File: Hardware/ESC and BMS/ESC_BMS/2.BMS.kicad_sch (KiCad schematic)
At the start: 39 parts, among them J301 SW IN, J302 SW OUT, Q301 SQJ141ELP, Q302 SQJ141ELP, Q303 FDV304P, Q304 PMV20XNEA, Q305 SQJ141ELP, U301 BQ2057W, U302 BQ2969

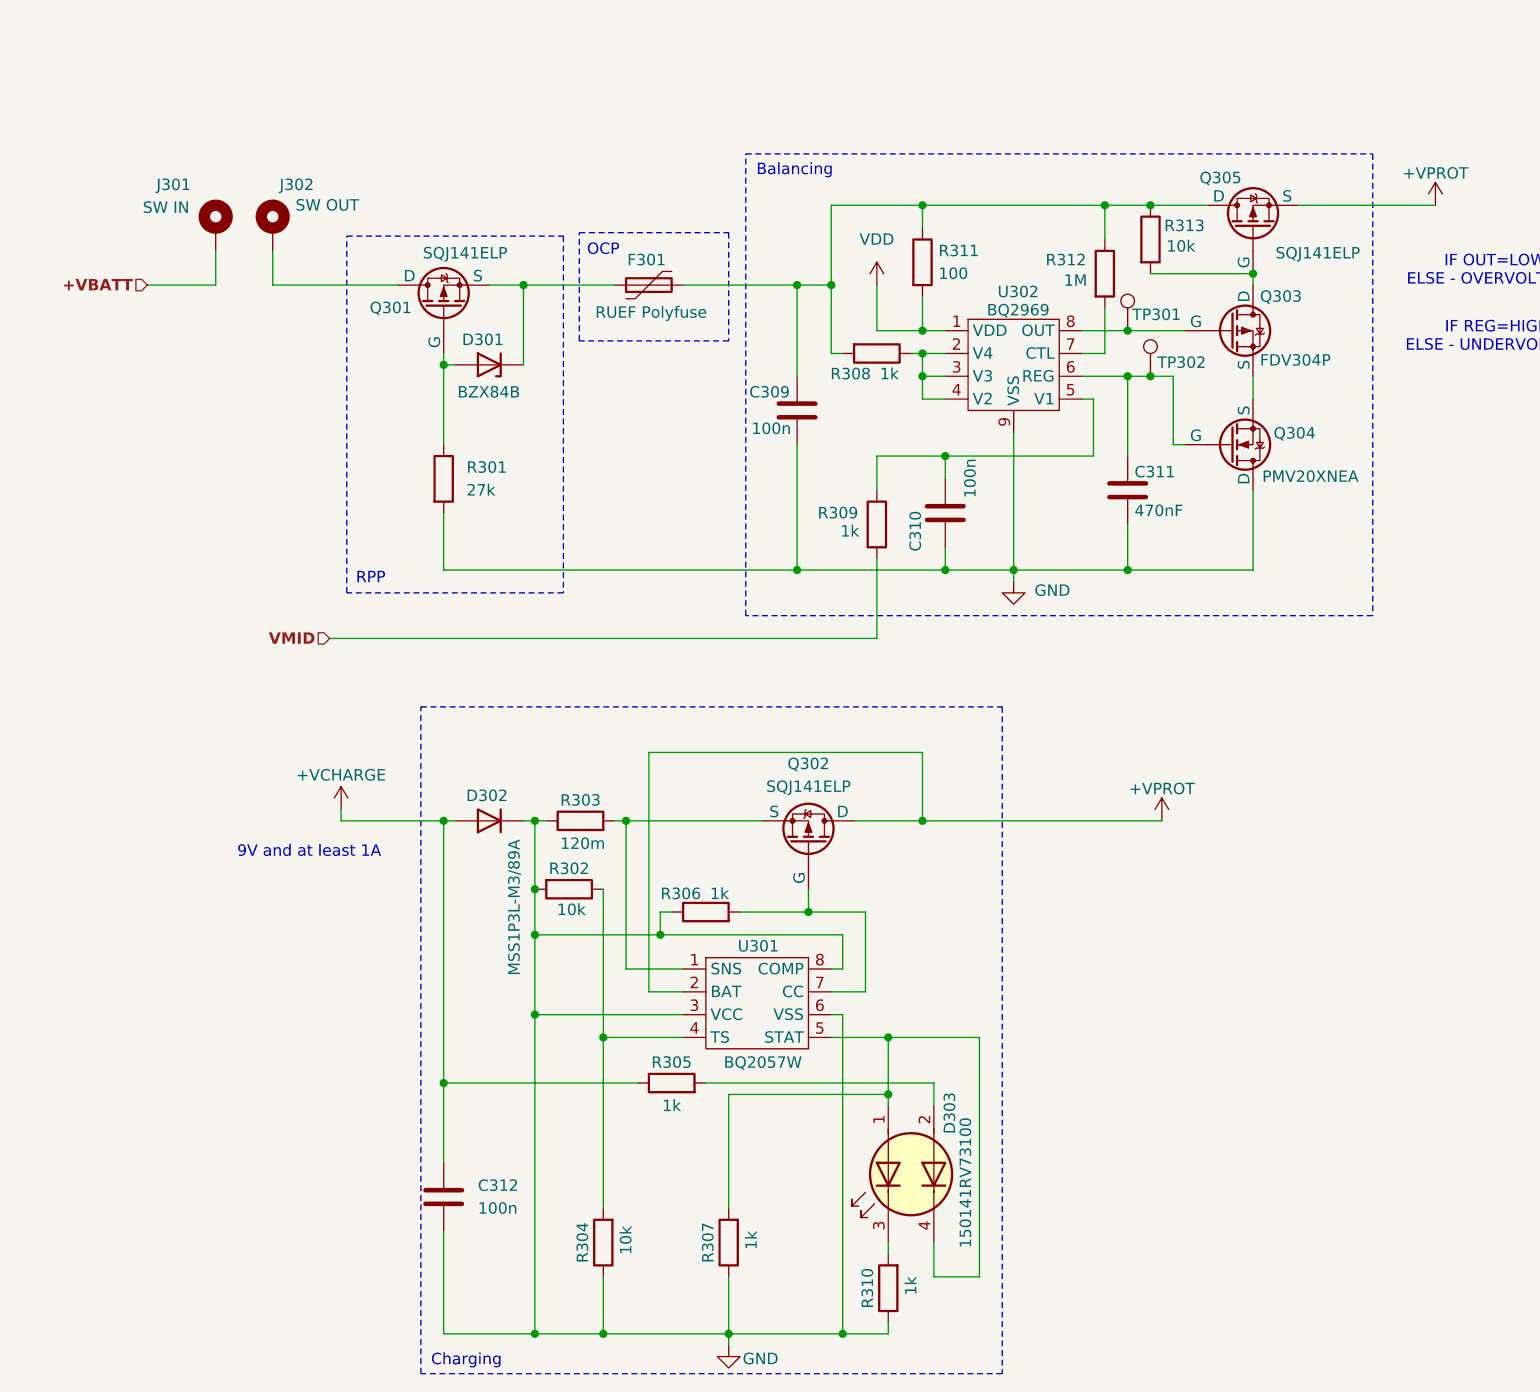
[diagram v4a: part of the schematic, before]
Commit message: ESC done
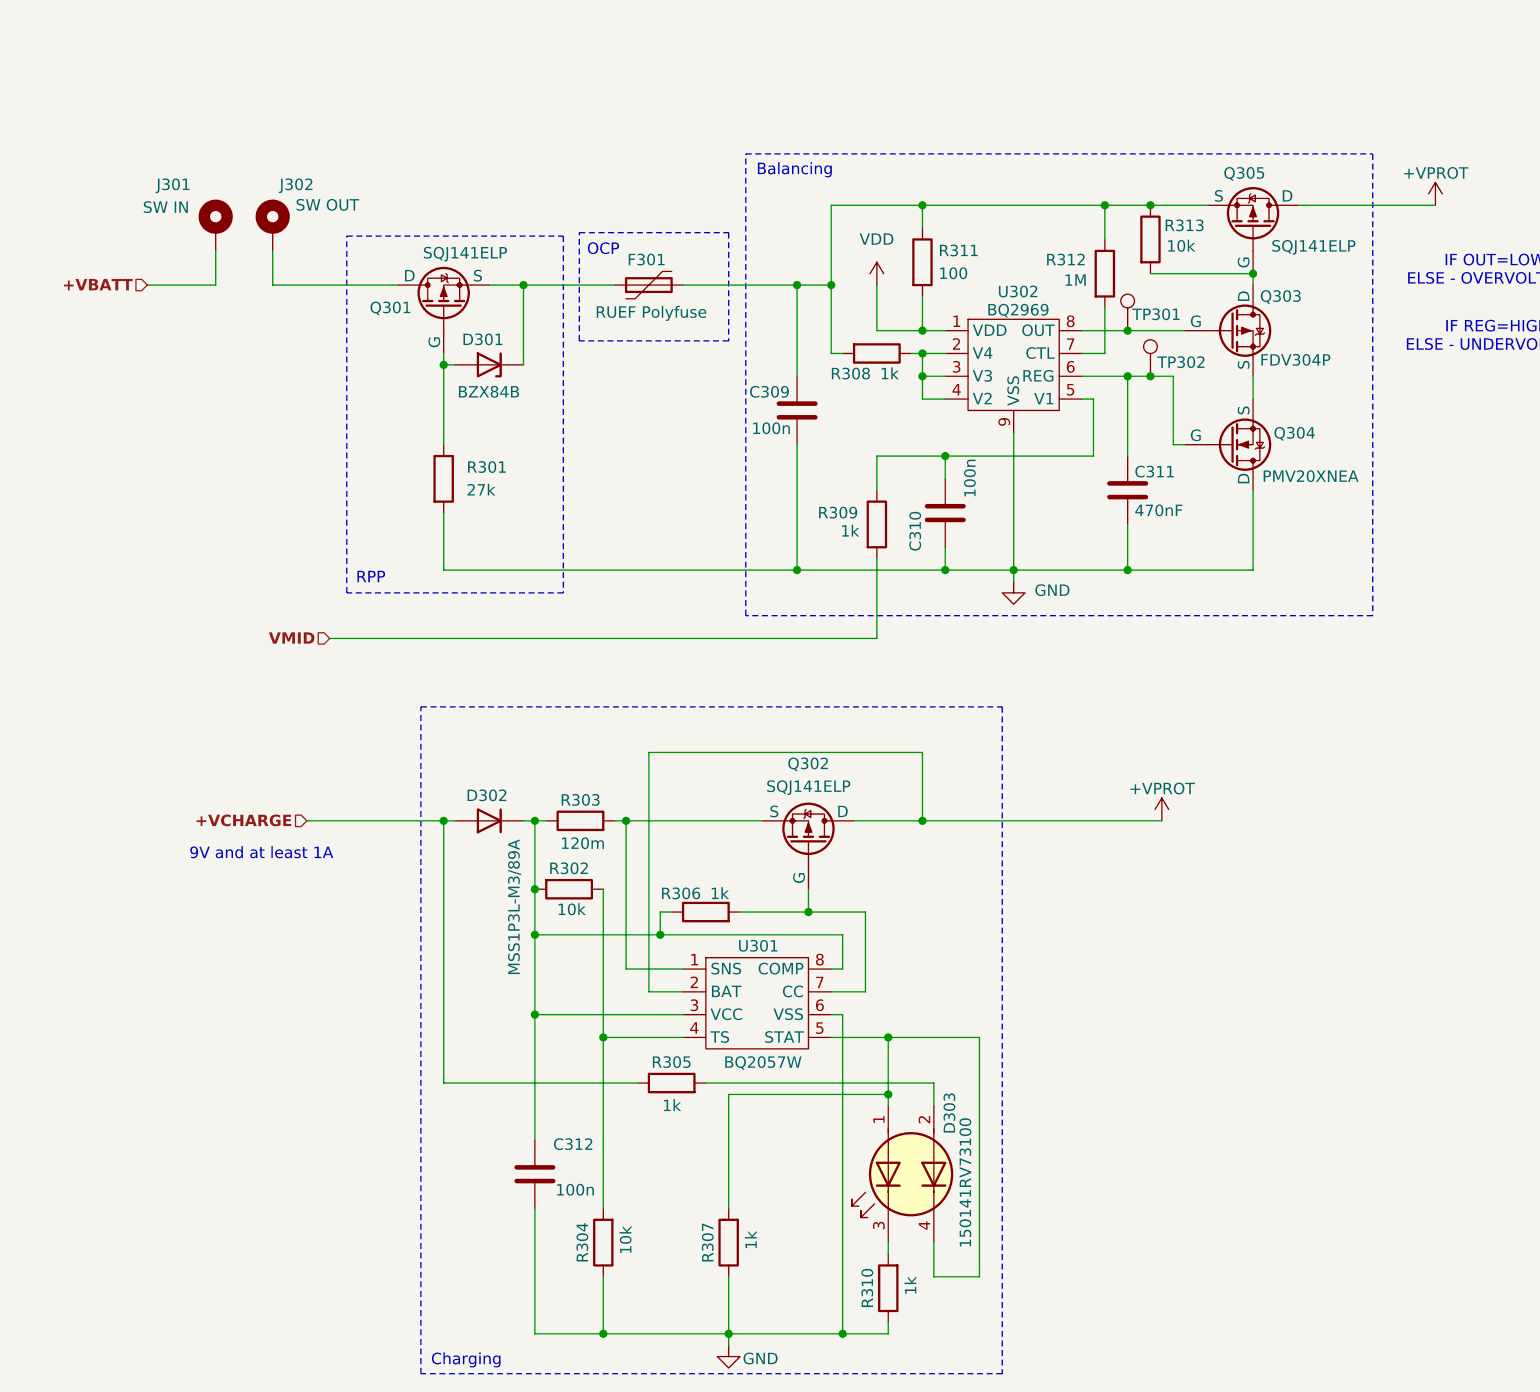
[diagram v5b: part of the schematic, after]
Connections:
- net +VCHARGE: no longer C312.1
- net +VPROT: now also Q305.1 (D); no longer Q305.3 (S)
- net GND: no longer D302.1 (K), R302.2, R303.1, R306.1, U301.3 (VCC), U301.8 (COMP)
- net at C309.1, F301.2, R308.2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: now also Q305.3 (S); no longer Q305.1 (D)
- new net: C312.1, D302.1 (K), R302.2, R303.1, R306.1, U301.3 (VCC), U301.8 (COMP)
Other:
- moved on the sheet: C312, Q305
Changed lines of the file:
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@@
 	(text "9V and at least 1A"
 		(exclude_from_sim no)
-		(at 147.574 158.496 0)
+		(at 142.24 158.75 0)
 		(effects
 			(font
@@
 	)
 	(junction
-		(at 172.72 176.53)
-		(diameter 0)
-		(color 0 0 0 0)
-	)
-	(junction
 		(at 241.3 105.41)
 		(diameter 0)
@@
 	)
 	(junction
-		(at 172.72 212.09)
+		(at 215.9 154.94)
 		(diameter 0)
 		(color 0 0 0 0)
 	)
 	(junction
-		(at 215.9 154.94)
+		(at 215.9 105.41)
 		(diameter 0)
 		(color 0 0 0 0)
 	)
 	(junction
-		(at 215.9 105.41)
+		(at 201.93 95.25)
 		(diameter 0)
 		(color 0 0 0 0)
 	)
 	(junction
-		(at 201.93 95.25)
+		(at 172.72 176.53)
 		(diameter 0)
 		(color 0 0 0 0)
@@
 		(color 0 0 0 0)
 	)
-	(junction
-		(at 162.56 184.15)
-		(diameter 0)
-		(color 0 0 0 0)
-	)
 	(wire
 		(pts
@@
 	(wire
 		(pts
-			(xy 151.13 154.94) (xy 162.56 154.94)
+			(xy 147.32 154.94) (xy 162.56 154.94)
 		)
 		(stroke
@@
 	(wire
 		(pts
-			(xy 162.56 104.14) (xy 162.56 113.03)
+			(xy 172.72 176.53) (xy 172.72 190.5)
 		)
 		(stroke
@@
 	(wire
 		(pts
-			(xy 129.54 36.83) (xy 142.24 36.83)
+			(xy 162.56 104.14) (xy 162.56 113.03)
 		)
 		(stroke
@@
 	(wire
 		(pts
-			(xy 172.72 176.53) (xy 172.72 212.09)
+			(xy 129.54 36.83) (xy 142.24 36.83)
 		)
 		(stroke
@@
 	(wire
 		(pts
-			(xy 162.56 193.04) (xy 162.56 184.15)
-		)
-		(stroke
-			(width 0)
-			(type default)
-		)
-	)
-	(wire
-		(pts
 			(xy 149.86 134.62) (xy 210.82 134.62)
 		)
@@
 	(wire
 		(pts
-			(xy 172.72 212.09) (xy 180.34 212.09)
-		)
-		(stroke
-			(width 0)
-			(type default)
-		)
-	)
-	(wire
-		(pts
 			(xy 236.22 90.17) (xy 236.22 86.36)
 		)
@@
 	(wire
 		(pts
-			(xy 151.13 153.67) (xy 151.13 154.94)
-		)
-		(stroke
-			(width 0)
-			(type default)
-		)
-	)
-	(wire
-		(pts
 			(xy 185.42 173.99) (xy 185.42 147.32)
 		)
@@
 	(wire
 		(pts
-			(xy 162.56 212.09) (xy 172.72 212.09)
+			(xy 201.93 95.25) (xy 205.74 95.25)
 		)
 		(stroke
@@
 	(wire
 		(pts
-			(xy 201.93 95.25) (xy 205.74 95.25)
+			(xy 226.06 127) (xy 238.76 127)
 		)
 		(stroke
@@
 	(wire
 		(pts
-			(xy 226.06 127) (xy 238.76 127)
+			(xy 22.86 31.75) (xy 22.86 33.02)
 		)
 		(stroke
@@
 	(wire
 		(pts
-			(xy 22.86 31.75) (xy 22.86 33.02)
+			(xy 143.51 95.25) (xy 157.48 95.25)
 		)
 		(stroke
@@
 	(wire
 		(pts
-			(xy 143.51 95.25) (xy 157.48 95.25)
+			(xy 217.17 201.93) (xy 217.17 205.74)
 		)
 		(stroke
@@
 	(wire
 		(pts
-			(xy 217.17 201.93) (xy 217.17 205.74)
+			(xy 172.72 198.12) (xy 172.72 212.09)
 		)
 		(stroke
@@
 	(wire
 		(pts
+			(xy 172.72 212.09) (xy 180.34 212.09)
+		)
+		(stroke
+			(width 0)
+			(type default)
+		)
+	)
+	(wire
+		(pts
 			(xy 238.76 100.33) (xy 245.11 100.33)
 		)
@@
 	(wire
 		(pts
-			(xy 162.56 200.66) (xy 162.56 212.09)
-		)
-		(stroke
-			(width 0)
-			(type default)
-		)
-	)
-	(wire
-		(pts
 			(xy 162.56 184.15) (xy 184.15 184.15)
 		)
@@
 		)
 	)
+	(hierarchical_label "+VCHARGE"
+		(shape input)
+		(at 147.32 154.94 180)
+		(effects
+			(font
+				(size 1.27 1.27)
+				(thickness 0.254)
+				(bold yes)
+			)
+			(justify right)
+		)
+	)
 	(symbol
 		(lib_id "power:+3.3V")
@@
 	(symbol
 		(lib_id "Simulation_SPICE:PMOS")
-		(at 252.73 88.9 90)
+		(at 252.73 88.9 270)
+		(mirror x)
 		(unit 1)
 		(exclude_from_sim no)
@@
 		(dnp no)
 		(property "Reference" "Q305"
-			(at 251.46 83.312 90)
+			(at 249.428 82.804 90)
 			(effects
 				(font
@@
 		)
 		(property "Value" "SQJ141ELP"
-			(at 264.668 91.694 90)
+			(at 254.762 90.932 90)
 			(effects
 				(font
@@
 		)
 		(property "Footprint" "Package_SO:PowerPAK_SO-8L_Single"
-			(at 250.19 83.82 0)
+			(at 255.27 83.82 0)
 			(effects
 				(font
@@
 		)
 		(property "Datasheet" "https://docs.rs-online.com/afb1/A700000014240545.pdf"
-			(at 265.43 88.9 0)
+			(at 240.03 88.9 0)
 			(effects
 				(font
@@
 		)
 		(property "Sim.Device" "PMOS"
-			(at 269.875 88.9 0)
+			(at 235.585 88.9 0)
 			(effects
 				(font
@@
 		)
 		(property "Sim.Type" "VDMOS"
-			(at 271.78 88.9 0)
+			(at 233.68 88.9 0)
 			(effects
 				(font
@@
 		)
 		(property "Sim.Pins" "1=D 2=G 3=S"
-			(at 267.97 88.9 0)
+			(at 237.49 88.9 0)
 			(effects
 				(font
@@
 	(symbol
 		(lib_id "power:VBUS")
-		(at 151.13 153.67 0)
-		(unit 1)
-		(exclude_from_sim no)
-		(in_bom yes)
-		(on_board yes)
-		(dnp no)
-		(property "Reference" "#PWR0407"
-			(at 151.13 157.48 0)
-			(effects
-				(font
-					(size 1.27 1.27)
-				)
-				(hide yes)
-			)
-		)
-		(property "Value" "+VCHARGE"
-			(at 151.13 149.86 0)
-			(effects
-				(font
-					(size 1.27 1.27)
-				)
-			)
-		)
-		(property "Footprint" ""
-			(at 151.13 153.67 0)
-			(effects
-				(font
-					(size 1.27 1.27)
-				)
-				(hide yes)
-			)
-		)
-		(property "Datasheet" ""
-			(at 151.13 153.67 0)
-			(effects
-				(font
-					(size 1.27 1.27)
-				)
-				(hide yes)
-			)
-		)
-		(property "Description" "Power symbol creates a global label with name \"VBUS\""
-			(at 151.13 153.67 0)
-			(effects
-				(font
-					(size 1.27 1.27)
-				)
-				(hide yes)
-			)
-		)
-		(pin "1"
-		)
-		(instances
-			(project "SPROJ3EE_ESC_BMS"
-				(path "/64aee9f2-a448-43ef-b28d-f00e276bd9f5/eb2740b7-11f5-4644-9e72-e71a449b99af"
-					(reference "#PWR0407")
-					(unit 1)
-				)
-			)
-		)
-	)
-	(symbol
-		(lib_id "power:VBUS")
 		(at 273.05 86.36 0)
 		(unit 1)
@@
 	(symbol
 		(lib_id "Device:C")
-		(at 162.56 196.85 0)
+		(at 172.72 194.31 0)
 		(unit 1)
 		(exclude_from_sim no)
@@
 		(on_board yes)
 		(dnp no)
-		(fields_autoplaced yes)
 		(property "Reference" "C312"
-			(at 166.37 195.5799 0)
+			(at 174.752 191.008 0)
 			(effects
 				(font
@@
 		)
 		(property "Value" "100n"
-			(at 166.37 198.1199 0)
+			(at 175.006 196.088 0)
 			(effects
 				(font
@@
 		)
 		(property "Footprint" "Capacitor_SMD:C_0805_2012Metric_Pad1.18x1.45mm_HandSolder"
-			(at 163.5252 200.66 0)
+			(at 173.6852 198.12 0)
 			(effects
 				(font
@@
 		)
 		(property "Datasheet" "~"
-			(at 162.56 196.85 0)
+			(at 172.72 194.31 0)
 			(effects
 				(font
@@
 		)
 		(property "Description" "Unpolarized capacitor"
-			(at 162.56 196.85 0)
+			(at 172.72 194.31 0)
 			(effects
 				(font
